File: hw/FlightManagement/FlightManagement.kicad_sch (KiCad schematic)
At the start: 61 parts, among them J4 430450412, Q1 MMBT2222A, U1 YTS1C0033BBG01, U12 TPS54202DDC, U2 STM32L431RCTx, U3 MPU-6050, U4 LIS2MDL, U8 SN65HVD230, Y4 Crystal_GND24

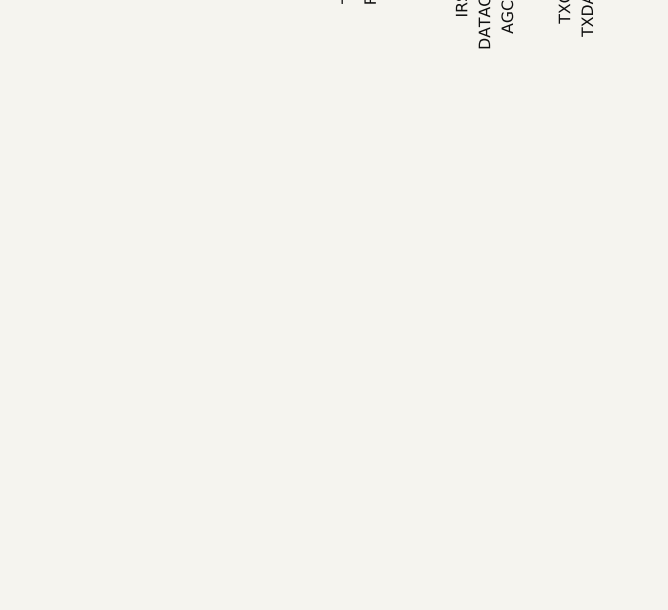
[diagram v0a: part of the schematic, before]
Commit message: add pdf outputs
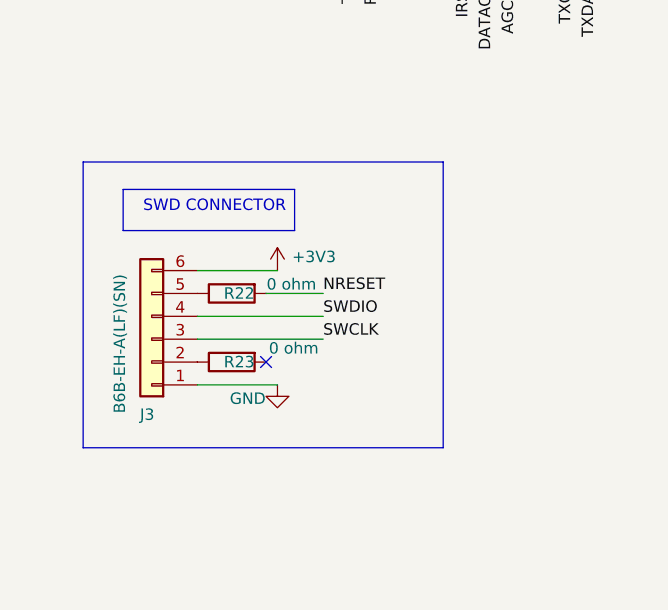
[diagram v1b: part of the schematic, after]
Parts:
- added J3: B6B-EH-A(LF)(SN), Connector_JST:JST_EH_B6B-EH-A_1x06_P2.50mm_Vertical, symbol Connector_Generic:Conn_01x06
- added R22, R23: 0 ohm, Resistor_SMD:R_0603_1608Metric_Pad0.98x0.95mm_HandSolder, symbol #inventree:RC0603FR-070RL
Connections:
- net +3V3: now also J3.6 (Pin_6)
- net GND: now also J3.1 (Pin_1)
- net NRESET: now also R22.2
- net SWCLK: now also J3.3 (Pin_3)
- net SWDIO: now also J3.4 (Pin_4)
- new net: J3.2 (Pin_2), R23.1
- new net: J3.5 (Pin_5), R22.1
- no-connect marks 1 -> 2
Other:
- company: (none) -> Daniel Enrique Pérez Díaz (steewBSD)
- title: (none) -> FlightManagementUnit

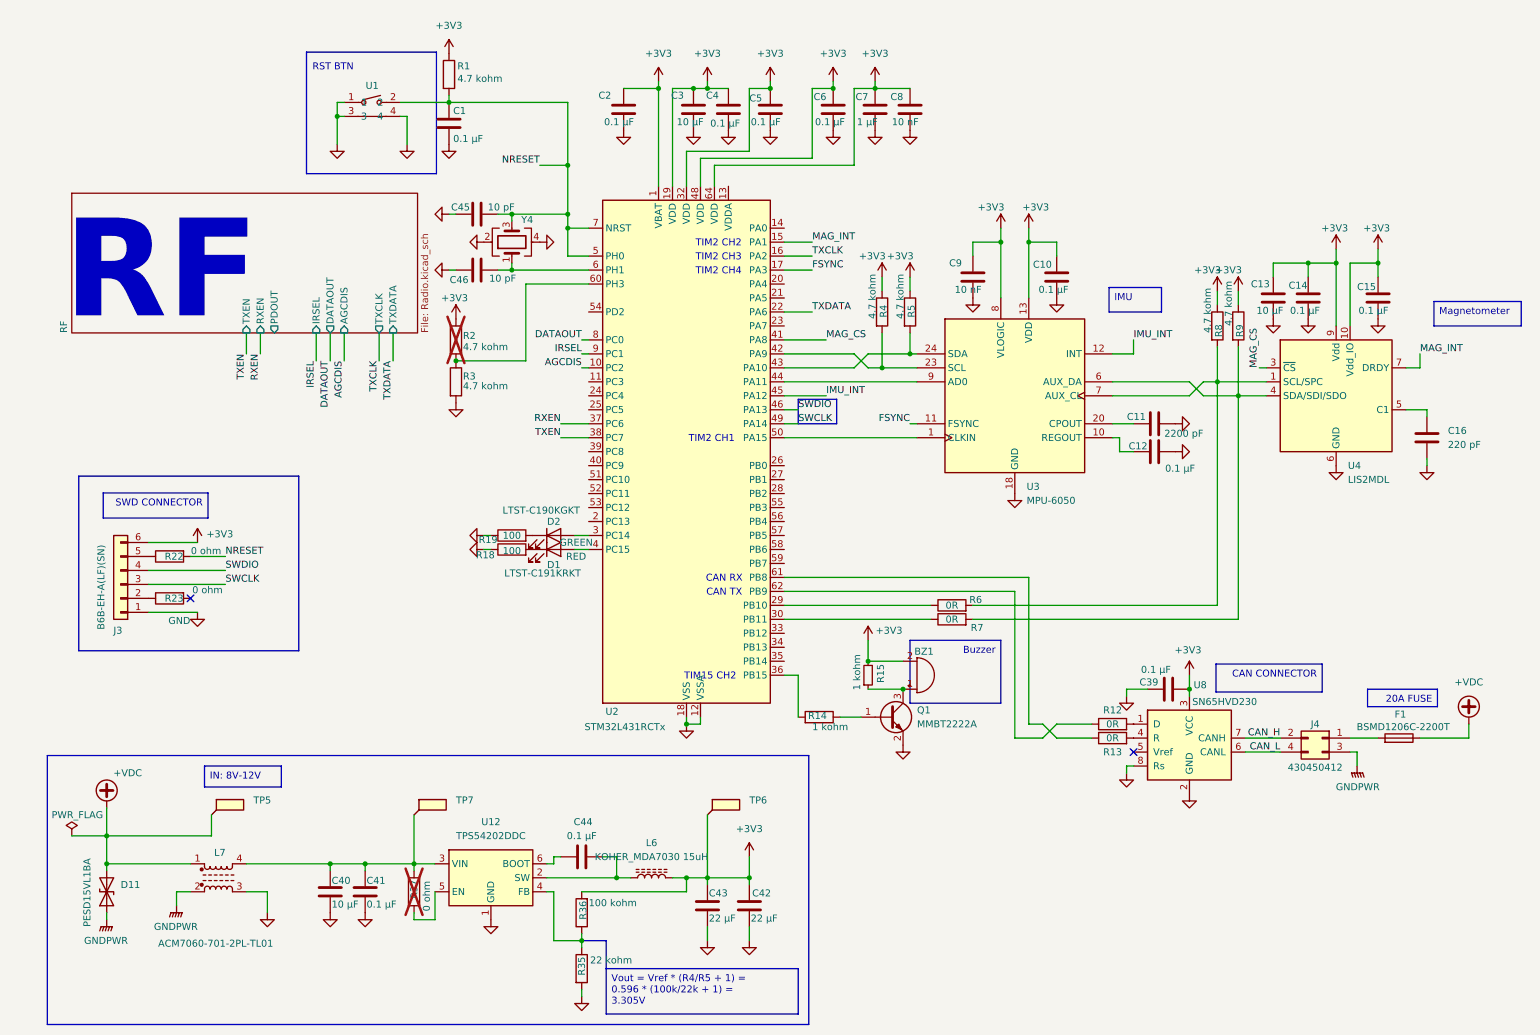
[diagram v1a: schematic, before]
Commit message: add NOR flash in FC
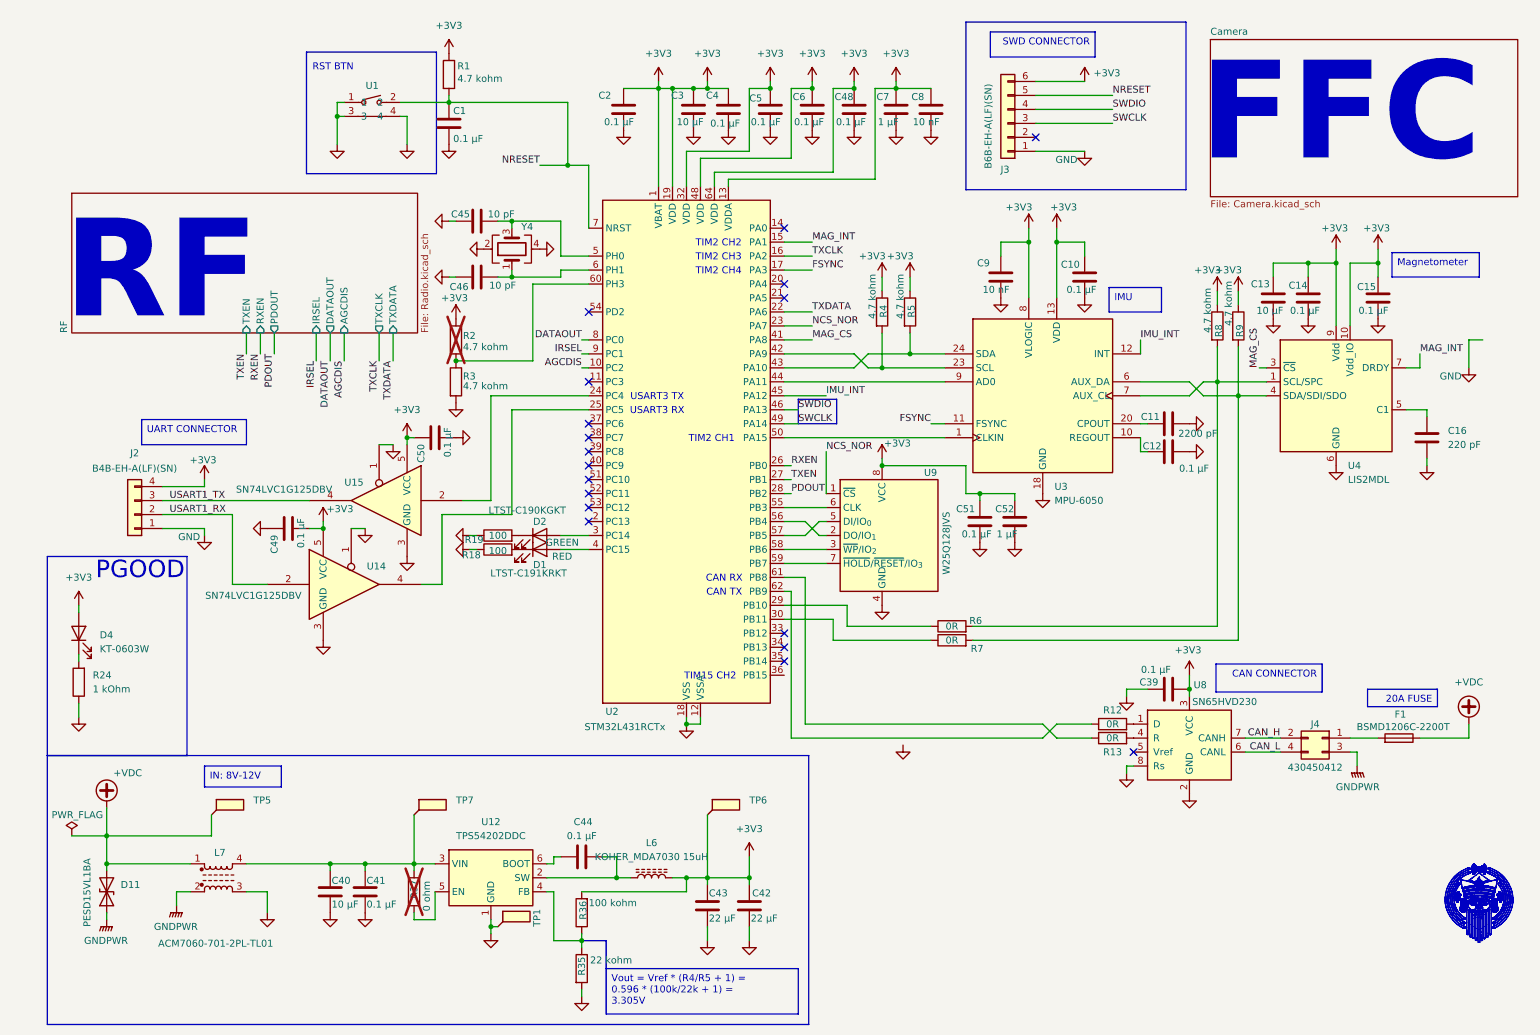
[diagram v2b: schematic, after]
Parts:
- removed BZ1: Buzzer, Buzzer_Beeper:Buzzer_TDK_PS1240P02BT_D12.2mm_H6.5mm, symbol Device:Buzzer
- removed Q1: MMBT2222A, Package_TO_SOT_SMD:SOT-23, symbol Transistor_BJT:MMBT2222A
- removed R14: 1 kohm, Resistor_SMD:R_0603_1608Metric_Pad0.98x0.95mm_HandSolder, symbol #inventree:RC0603FR-074K7L
- removed R15: 1 kohm, Resistor_SMD:R_0603_1608Metric_Pad0.98x0.95mm_HandSolder, symbol Device:R_Small
- removed R22, R23: 0 ohm, Resistor_SMD:R_0603_1608Metric_Pad0.98x0.95mm_HandSolder, symbol #inventree:RC0603FR-070RL
- added C48, C49, C50, C51: 0.1 µF, Capacitor_SMD:C_0603_1608Metric_Pad1.08x0.95mm_HandSolder, symbol #inventree:CL21B104KBCNNNC
- added C52: 1 µF, Capacitor_SMD:C_0603_1608Metric_Pad1.08x0.95mm_HandSolder, symbol #inventree:CL21B104KBCNNNC
- added D4: KT-0603W, LED_SMD:LED_0603_1608Metric_Pad1.05x0.95mm_HandSolder, symbol Device:LED
- added J2: B4B-EH-A(LF)(SN), Connector_JST:JST_EH_B4B-EH-A_1x04_P2.50mm_Vertical, symbol Connector_Generic:Conn_01x04
- added R24: 1 kOhm, Resistor_SMD:R_0603_1608Metric_Pad0.98x0.95mm_HandSolder, symbol Device:R
- added TP1: TestPoint_Flag, TestPoint:TestPoint_Pad_1.0x1.0mm, symbol Connector:TestPoint_Flag
- added U14, U15: SN74LVC1G125DBV, Package_TO_SOT_SMD:SOT-23-5_HandSoldering, symbol 74xGxx:SN74LVC1G125DBV
- added U9: W25Q128JVS, Package_SO:SOIC-8_5.3x5.3mm_P1.27mm, symbol Memory_Flash:W25Q128JVS
- C1, C10, C11, C12, C13, C14, C15, C16, C2, C3, C39, C4, C40, C41, C42, C43, C44, C45, C46, C5, C6, C7, C8, C9: footprint Capacitor_SMD:C_0805_2012Metric_Pad1.18x1.45mm_HandSolder -> Capacitor_SMD:C_0603_1608Metric_Pad1.08x0.95mm_HandSolder
- TP5, TP6, TP7: footprint TestPoint:TestPoint_Plated_Hole_D2.0mm -> TestPoint:TestPoint_Pad_1.0x1.0mm
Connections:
- net +3V3: now also U2.13 (VDDA), C48.2, C49.1, C50.2, C51.2, C52.2, D4.2 (A), J2.4 (Pin_4), U14.5 (VCC), U15.5 (VCC), U9.8 (VCC)
- net GND: now also C48.1, C49.2, C50.1, C51.1, C52.1, J2.1 (Pin_1), R24.1, TP1.1, U14.1, U14.3 (GND), U15.1, U15.3 (GND), U9.4 (GND)
- net NRESET: now also J3.5 (Pin_5); no longer C45.2, U2.5 (PH0), Y4.3
- net RXEN: now also U2.26 (PB0); no longer U2.37 (PC6)
- net TXEN: now also U2.27 (PB1); no longer U2.38 (PC7)
- net NCS_NOR: now reaches U2.23 (PA7)
- net NCS_NOR: now also U9.1 (~{CS})
- net at U2.24 (PC4): now also U15.2
- net at U2.25 (PC5): now also U14.4
- net PDOUT: now reaches U2.28 (PB2)
- net at U2.55 (PB3): now also U9.6 (CLK)
- net at U2.56 (PB4): now also U9.2 (DO/IO_{1})
- net at U2.57 (PB5): now also U9.5 (DI/IO_{0})
- net at U2.58 (PB6): now also U9.3 (~{WP}/IO_{2})
- net at U2.59 (PB7): now also U9.7 (~{HOLD}/~{RESET}/IO_{3})
- new net: D4.1 (K), R24.2
- new net: C45.2, U2.5 (PH0), Y4.3
- new net USART1_RX: J2.2 (Pin_2), U14.2
- new net USART1_TX: J2.3 (Pin_3), U15.4
- no-connect marks 2 -> 18
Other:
- added sheet Camera (Camera.kicad_sch)
- note added: "FFC"
- note added: "PGOOD"
- note added: "USART3 RX"
- note added: "USART3 TX"
- moved on the sheet: C10, C11, C12, C45, C46, C6, C7, C8, C9, D1, D2, J3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

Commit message: final FC placement
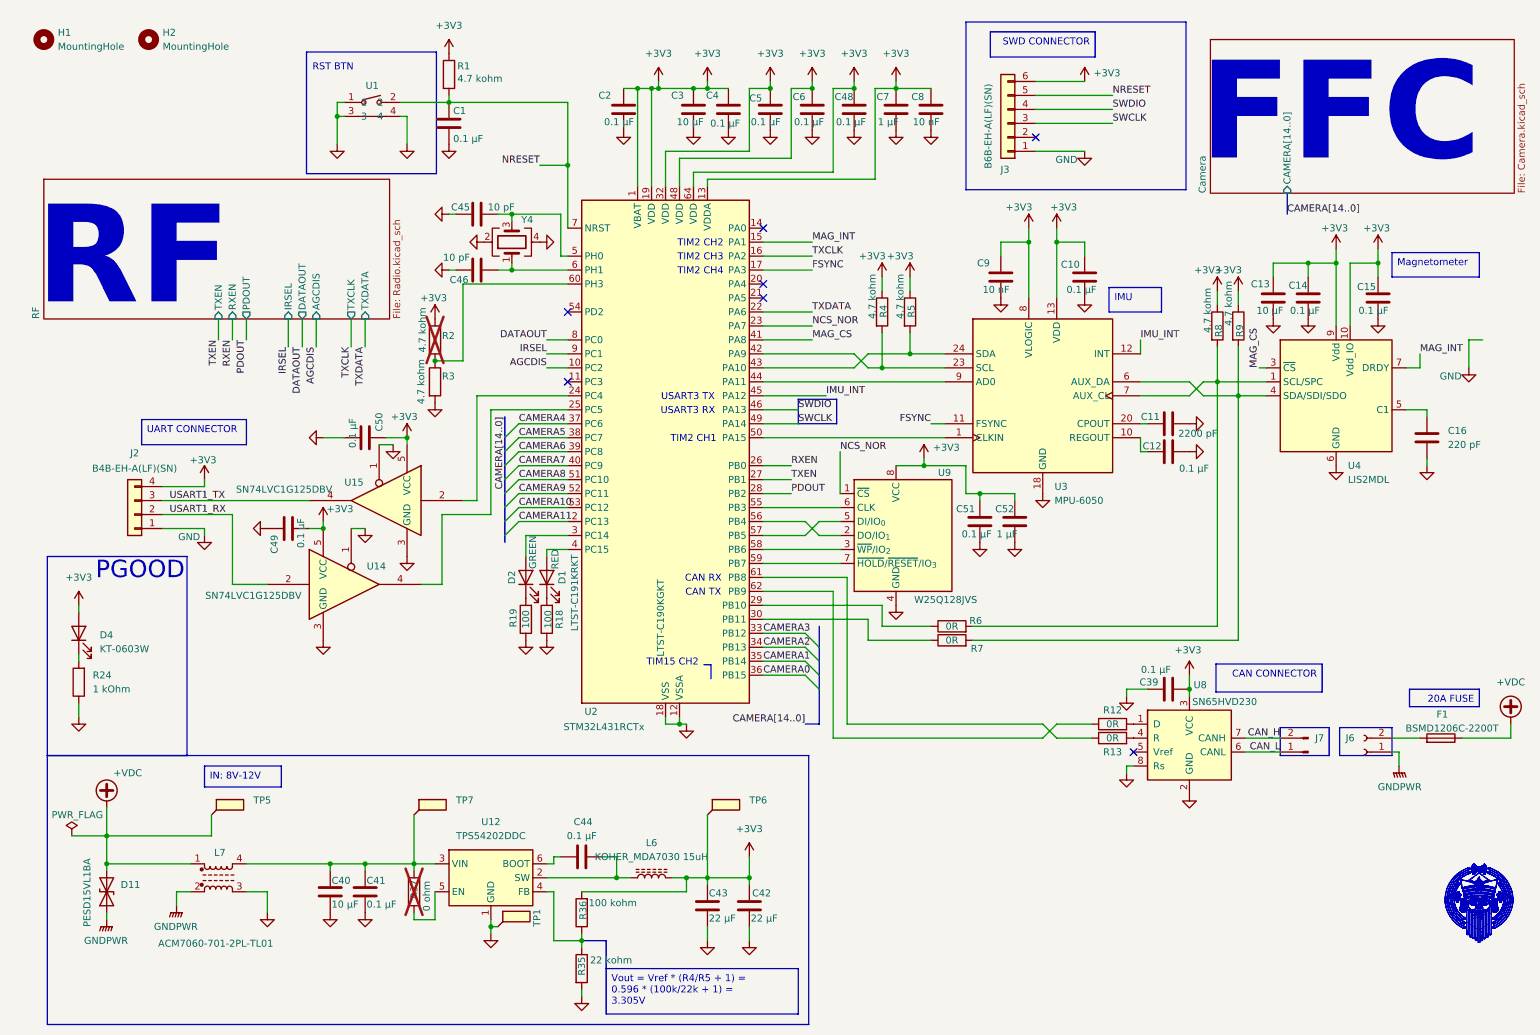
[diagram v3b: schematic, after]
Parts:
- removed J4: 430450412, Connector_Molex:Molex_Micro-Fit_3.0_43045-0412_2x02_P3.00mm_Vertical, symbol Connector_Generic:Conn_02x02_Odd_Even
- added H1, H2: MountingHole, MountingHole:MountingHole_2.2mm_M2, symbol Mechanical:MountingHole
- added J6: Conn_01x02_Socket, steew:JST_VL_B02P-VL_1x02_P6.2mm_Vertical, symbol Connector:Conn_01x02_Socket
- added J7: Conn_01x02_Pin, Connector_JST:JST_XH_B2B-XH-A_1x02_P2.50mm_Vertical, symbol Connector:Conn_01x02_Pin
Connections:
- net CAN_H: now also J7.2 (Pin_2)
- net CAN_L: now also J7.1 (Pin_1)
- net GNDPWR: now also J6.1 (Pin_1)
- net at F1.2: now also J6.2 (Pin_2)
- net CAMERA11: now reaches U2.2 (PC13)
- net CAMERA3: now reaches U2.33 (PB12)
- net CAMERA2: now reaches U2.34 (PB13)
- net CAMERA1: now reaches U2.35 (PB14)
- net CAMERA0: now reaches U2.36 (PB15)
- net CAMERA4: now reaches U2.37 (PC6)
- net CAMERA5: now reaches U2.38 (PC7)
- net CAMERA6: now reaches U2.39 (PC8)
- net CAMERA7: now reaches U2.40 (PC9)
- net CAMERA8: now reaches U2.51 (PC10)
- net CAMERA9: now reaches U2.52 (PC11)
- net CAMERA10: now reaches U2.53 (PC12)
- no-connect marks 18 -> 7
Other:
- sheet Camera ports: added CAMERA[14..0]; removed none
- moved on the sheet: C45, C46, C50, D1, D2, F1, R18, R19, R2, R3, U2, U9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

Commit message: preliminar design for battery power monitor, add sd card to fmu
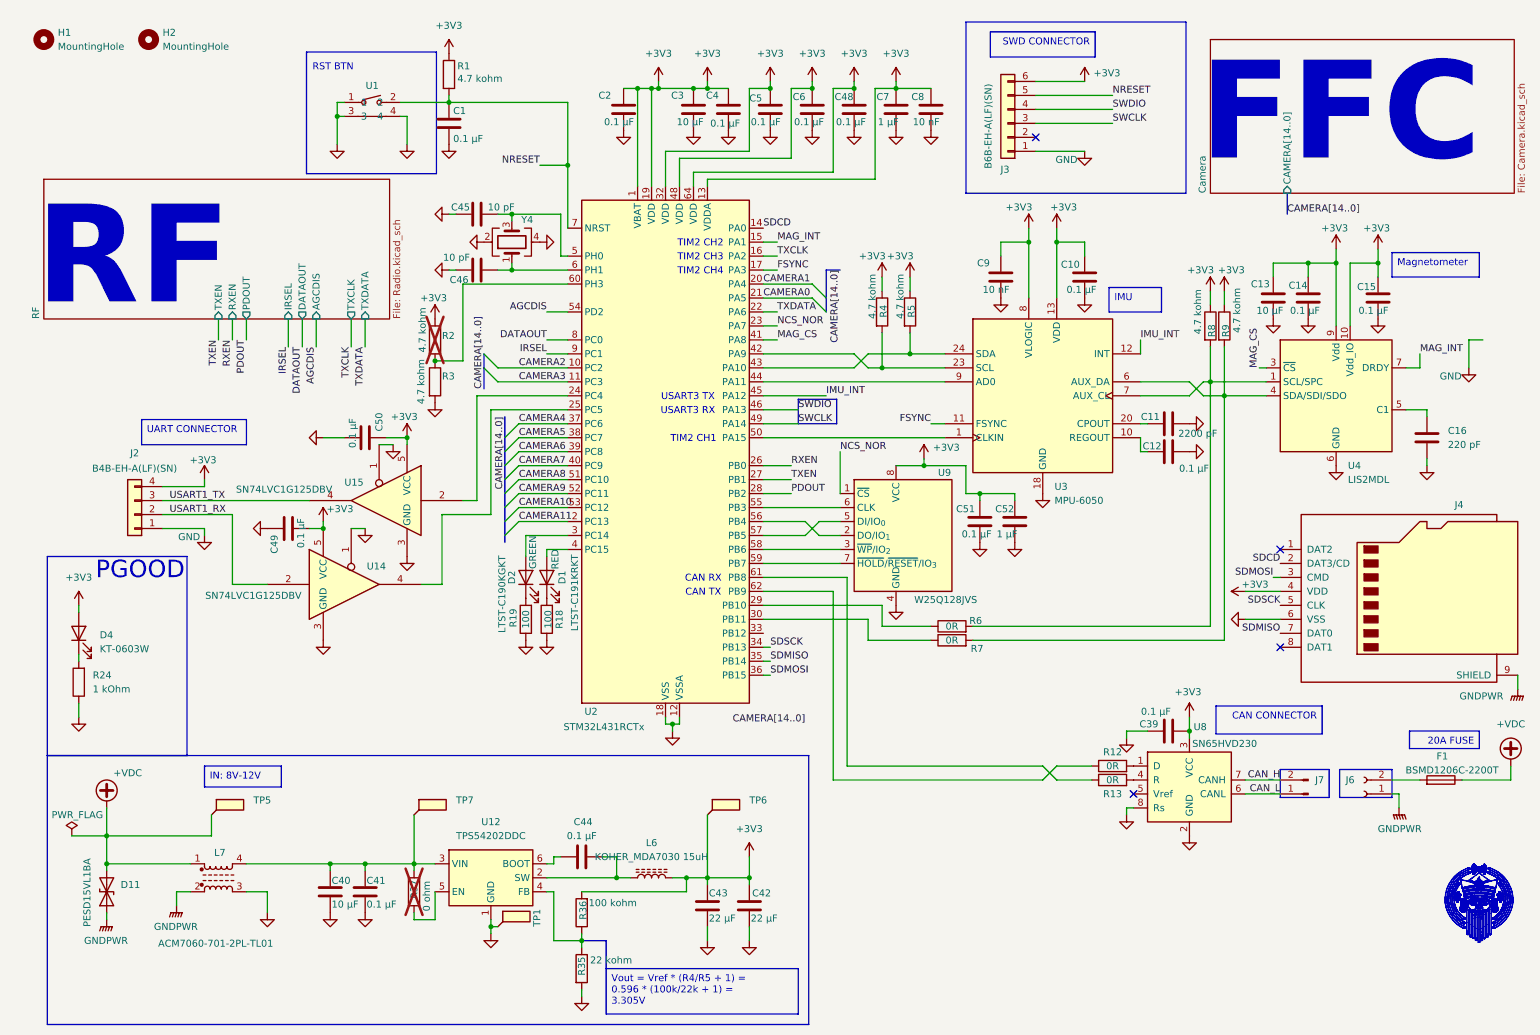
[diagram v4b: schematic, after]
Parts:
- added J4: Micro_SD_Card, Connector_Card:microSD_HC_Molex_47219-2001, symbol Connector:Micro_SD_Card
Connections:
- net +3V3: now also J4.4 (VDD)
- net AGCDIS: now also U2.54 (PD2); no longer U2.10 (PC2)
- net CAMERA0: now also U2.21 (PA5); no longer U2.36 (PB15)
- net CAMERA1: now also U2.20 (PA4); no longer U2.35 (PB14)
- net CAMERA2: now also U2.10 (PC2); no longer U2.34 (PB13)
- net CAMERA3: now also U2.11 (PC3); no longer U2.33 (PB12)
- net GND: now also J4.6 (VSS)
- net GNDPWR: now also J4.9 (SHIELD)
- net SDCD: now reaches U2.14 (PA0)
- net SDCD: now also J4.2 (DAT3/CD)
- new net SDMISO: J4.7 (DAT0), U2.35 (PB14)
- new net SDMOSI: J4.3 (CMD), U2.36 (PB15)
- new net SDSCK: J4.5 (CLK), U2.34 (PB13)
- no-connect marks 7 -> 4
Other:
- note removed: "TIM15 CH2"
- moved on the sheet: C39, F1, J6, J7, R12, R13, R8, R9, U8
